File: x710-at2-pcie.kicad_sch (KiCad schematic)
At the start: 10 parts, among them U4 EZX710AT2_S_LMR5

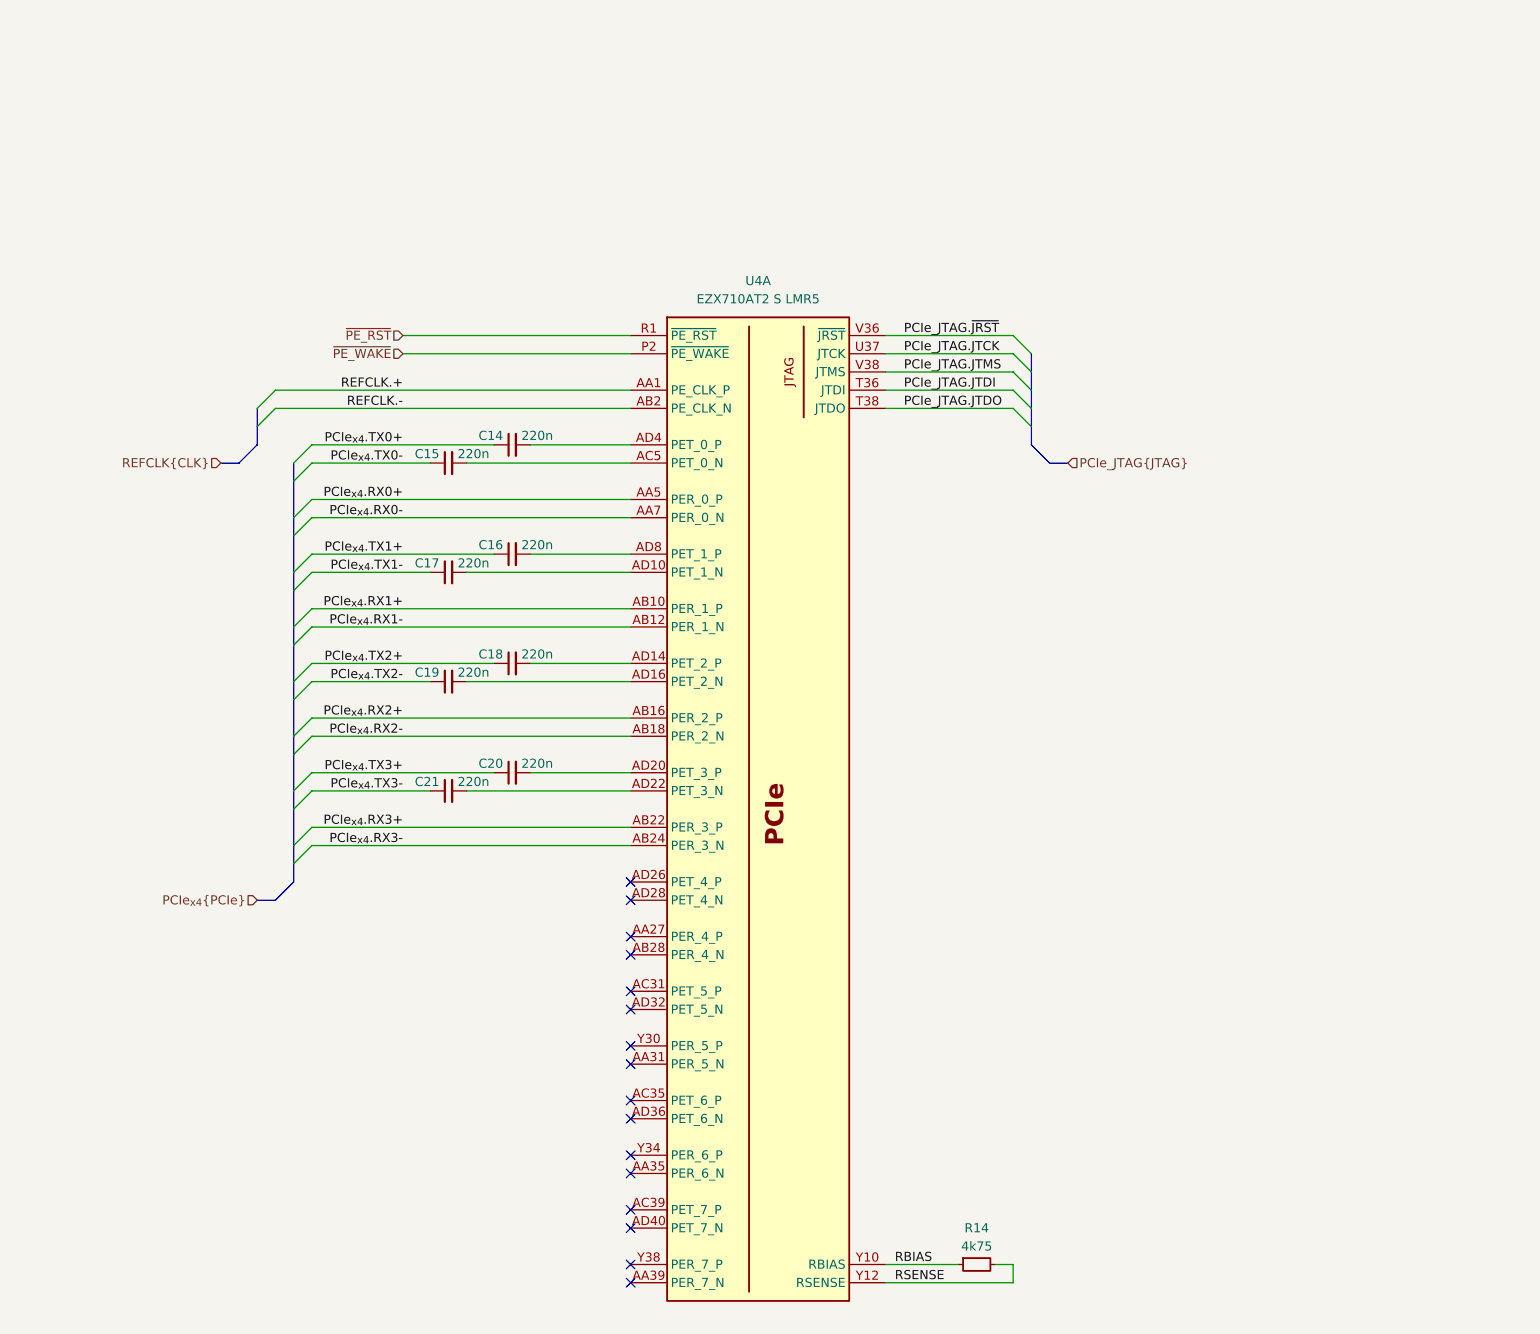
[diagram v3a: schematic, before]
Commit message: [#80813] Improve schematic readability, add debug connectors and missing resistors
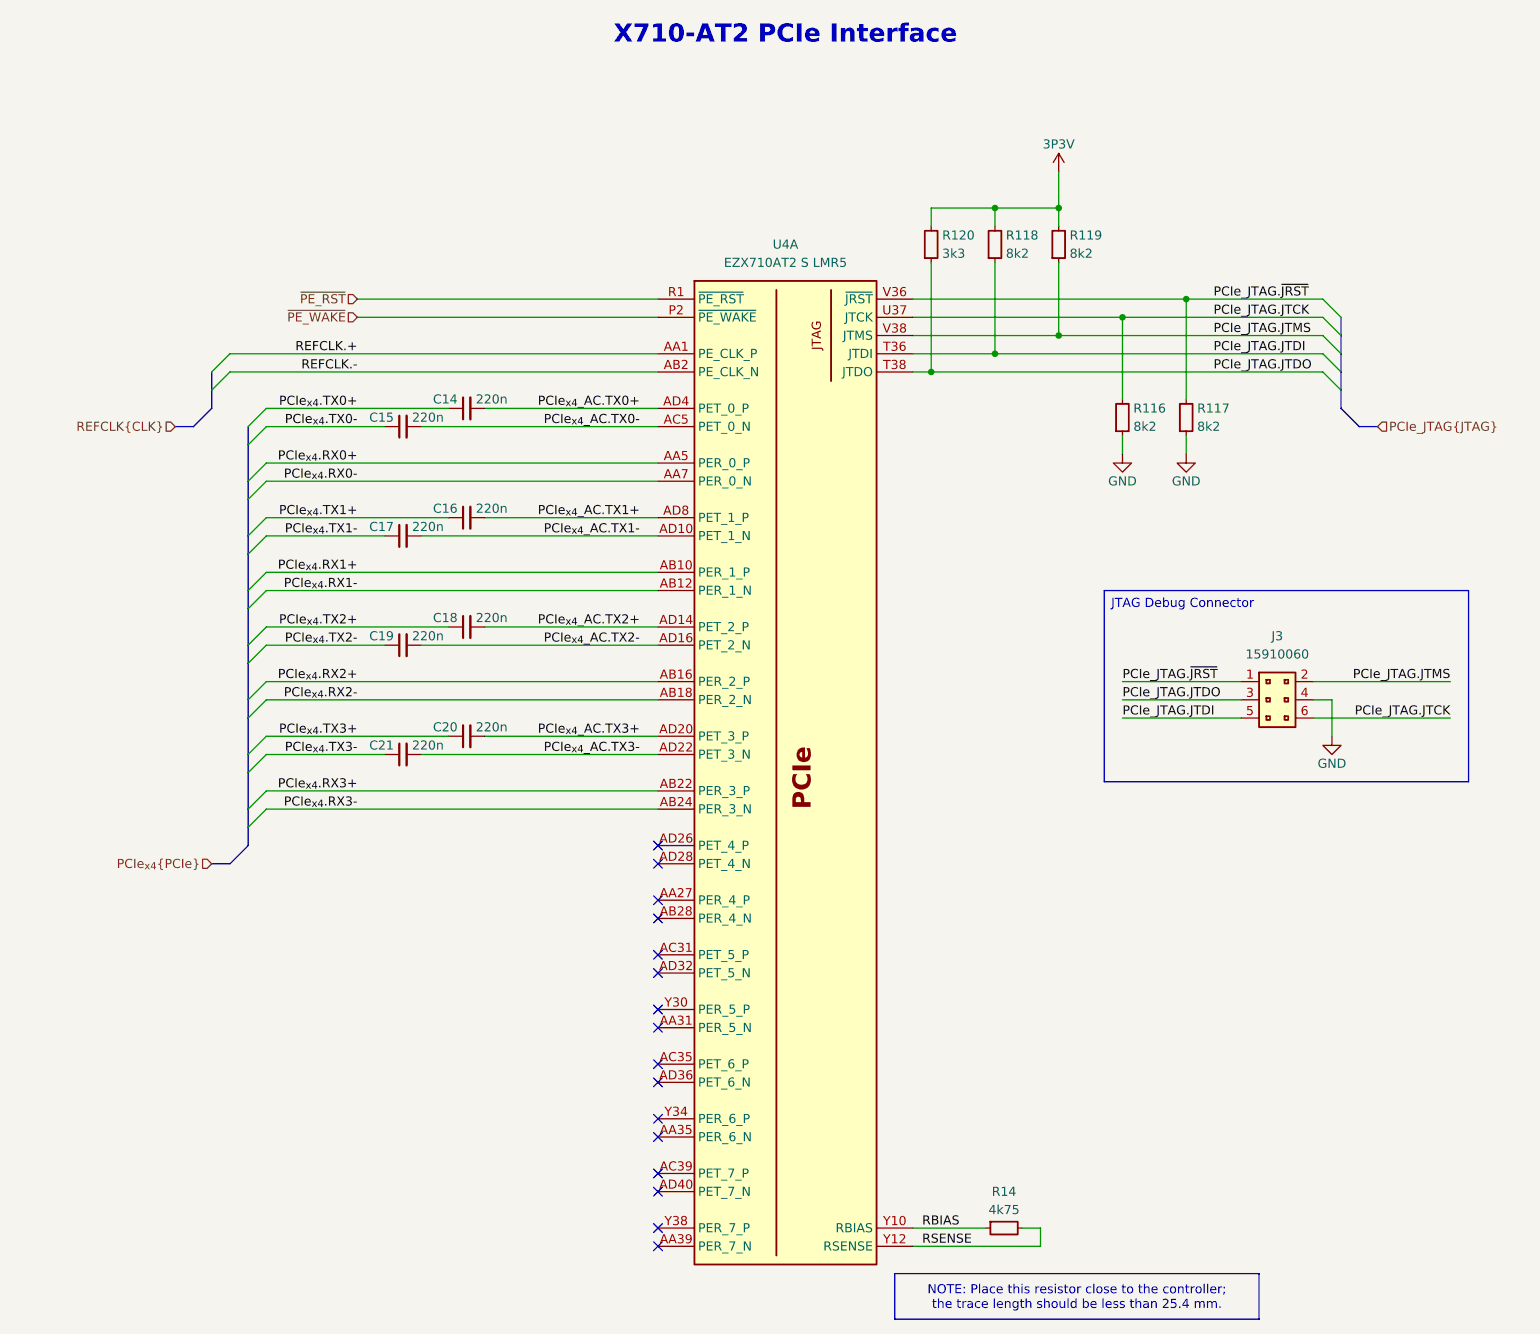
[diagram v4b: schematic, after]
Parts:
- added J3: PinHeader_2x3_P2.54mm_SMD, antmicro-footprints:PinHeader_2x3_P2.54mm_SMD, symbol antmicroGenericPinHeaders:PinHeader_2x3_P2.54mm_SMD
- added R116, R117, R118, R119: R_8k2_0402, antmicro-footprints:R_0402_1005Metric, symbol antmicroResistors0402:R_8k2_0402
- added R120: R_3k3_0402, antmicro-footprints:R_0402_1005Metric, symbol antmicroResistors0402:R_3k3_0402
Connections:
- net PCIe_JTAG.JTCK: now also J3.6, R116.2
- net PCIe_JTAG.JTDI: now also J3.5, R118.1
- net PCIe_JTAG.JTDO: now also J3.3, R120.1
- net PCIe_JTAG.JTMS: now also J3.2, R119.1
- net PCIe_JTAG.~{JRST}: now also J3.1, R117.2
- net PCIe_{x4}_AC.TX3+: now reaches C20.2, U4.AD20 (PET_3_P)
- net PCIe_{x4}_AC.TX2+: now reaches C18.2, U4.AD14 (PET_2_P)
- net PCIe_{x4}_AC.TX2-: now reaches C19.2, U4.AD16 (PET_2_N)
- net PCIe_{x4}_AC.TX0-: now reaches C15.2, U4.AC5 (PET_0_N)
- net PCIe_{x4}_AC.TX1-: now reaches C17.2, U4.AD10 (PET_1_N)
- net PCIe_{x4}_AC.TX0+: now reaches C14.2, U4.AD4 (PET_0_P)
- net PCIe_{x4}_AC.TX1+: now reaches C16.2, U4.AD8 (PET_1_P)
- net PCIe_{x4}_AC.TX3-: now reaches C21.2, U4.AD22 (PET_3_N)
- new net 3P3V: R118.2, R119.2, R120.2
- new net GND: J3.4, R116.1, R117.1
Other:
- note added: "X710-AT2 PCIe Interface"
- moved on the sheet: C14, C15, C16, C17, C18, C19, C20, C21, R14, U4A

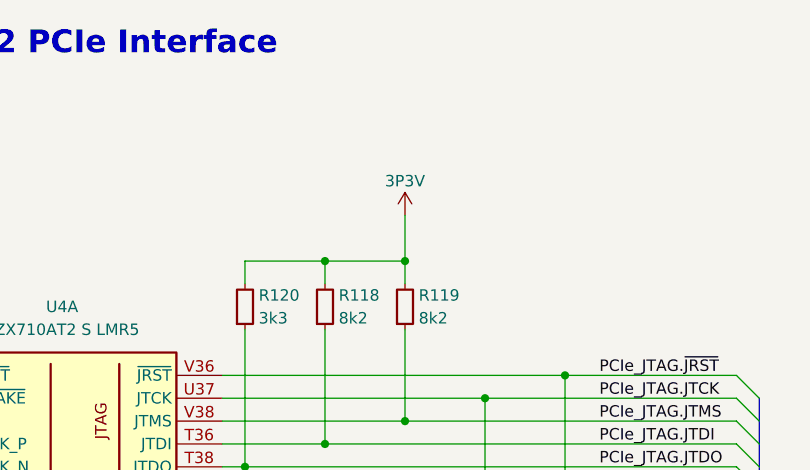
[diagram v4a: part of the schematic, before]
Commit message: [#80813] Change 3V3 and 1V88 power rails names
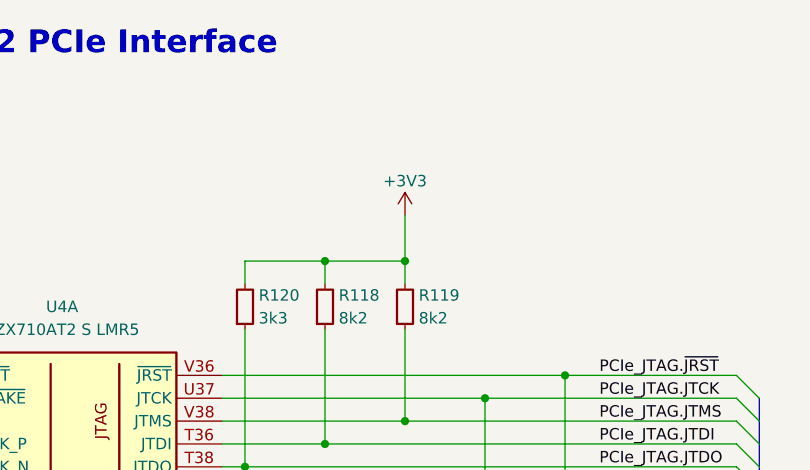
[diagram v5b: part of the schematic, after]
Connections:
- net 3P3V renamed +3V3
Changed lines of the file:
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@@
+	)
+	(symbol
+		(lib_id "antmicropower:+3V3")
+		(at 254 69.85 0)
+		(unit 1)
+		(exclude_from_sim no)
+		(in_bom yes)
+		(on_board yes)
+		(dnp no)
+		(property "Reference" "#PWR0125"
+			(at 269.24 69.85 0)
+			(effects
+				(font
+					(size 1.27 1.27)
+					(thickness 0.15)
+				)
+				(justify left bottom)
+				(hide yes)
+			)
+		)
+		(property "Value" "+3V3"
+			(at 254 66.04 0)
+			(effects
+				(font
+					(size 1.27 1.27)
+					(thickness 0.15)
+				)
+			)
+		)
+		(property "Footprint" ""
+			(at 269.24 77.47 0)
+			(effects
+				(font
+					(size 1.27 1.27)
+					(thickness 0.15)
+				)
+				(justify left bottom)
+				(hide yes)
+			)
+		)
+		(property "Datasheet" ""
+			(at 269.24 80.01 0)
+			(effects
+				(font
+					(size 1.27 1.27)
+					(thickness 0.15)
+				)
+				(justify left bottom)
+				(hide yes)
+			)
+		)
+		(property "Description" ""
+			(at 254 69.85 0)
+			(effects
+				(font
+					(size 1.27 1.27)
+				)
+				(hide yes)
+			)
+		)
+		(property "Author" "Antmicro"
+			(at 269.24 72.39 0)
+			(effects
+				(font
+					(size 1.27 1.27)
+					(thickness 0.15)
+				)
+				(justify left bottom)
+				(hide yes)
+			)
+		)
+		(property "License" "Apache-2.0"
+			(at 269.24 74.93 0)
+			(effects
+				(font
+					(size 1.27 1.27)
+					(thickness 0.15)
+				)
+				(justify left bottom)
+				(hide yes)
+			)
+		)
+		(pin "1"
+		)
+		(instances
+			(project "10-gbe-expansion"
+				(path "/04bda987-e5eb-48b4-9e90-d8211dc11b39/2e3e9f9b-8e60-4e62-87df-aa866913a2fb"
+					(reference "#PWR0125")
+					(unit 1)
+				)
+			)
+		)
 	)
 	(symbol
@@
 					(unit 1)
 				)
-			)
-		)
-	)
-	(symbol
-		(lib_id "antmicropower:VCC")
-		(at 254 69.85 0)
-		(unit 1)
-		(exclude_from_sim no)
-		(in_bom yes)
-		(on_board yes)
-		(dnp no)
-		(property "Reference" "#PWR0125"
-			(at 254 73.66 0)
-			(effects
-				(font
-					(size 1.27 1.27)
-				)
-				(hide yes)
-			)
-		)
-		(property "Value" "3P3V"
-			(at 254 66.04 0)
-			(effects
-				(font
-					(size 1.27 1.27)
-				)
-			)
-		)
-		(property "Footprint" ""
-			(at 254 69.85 0)
-			(effects
-				(font
-					(size 1.27 1.27)
-				)
-				(hide yes)
-			)
-		)
-		(property "Datasheet" ""
-			(at 254 69.85 0)
-			(effects
-				(font
-					(size 1.27 1.27)
-				)
-				(hide yes)
-			)
-		)
-		(property "Description" ""
-			(at 254 69.85 0)
-			(effects
-				(font
-					(size 1.27 1.27)
-				)
-				(hide yes)
-			)
-		)
-		(pin "1"
-		)
-		(instances
-			(project "10-gbe-expansion"
-				(path "/04bda987-e5eb-48b4-9e90-d8211dc11b39/2e3e9f9b-8e60-4e62-87df-aa866913a2fb"
-					(reference "#PWR0125")
-					(unit 1)
-				)
